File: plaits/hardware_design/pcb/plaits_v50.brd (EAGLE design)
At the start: 59 x 106.7 mm, 162 parts, among them IC1 R-78E3.3-0.5, IC2 TLC59281DBQ, IC3 LD2981ABU33, IC4 STM32F373CCT6, IC5 PCM5100APW, IC6 MCP6004, IC7 MCP6004, IC8 TL072PW, IC9 LM4040B10, J1 PJ301_THONKICONN6, J10 PJ301_THONKICONN6, J2 PJ301_THONKICONN6, J3 PJ301_THONKICONN6, J4 PJ301_THONKICONN6, J5 PJ301_THONKICONN6, J6 PJ301_THONKICONN6, J7 PJ301_THONKICONN6, J8 PJ301_THONKICONN6, J9 PJ301_THONKICONN6, Q1 8MHz

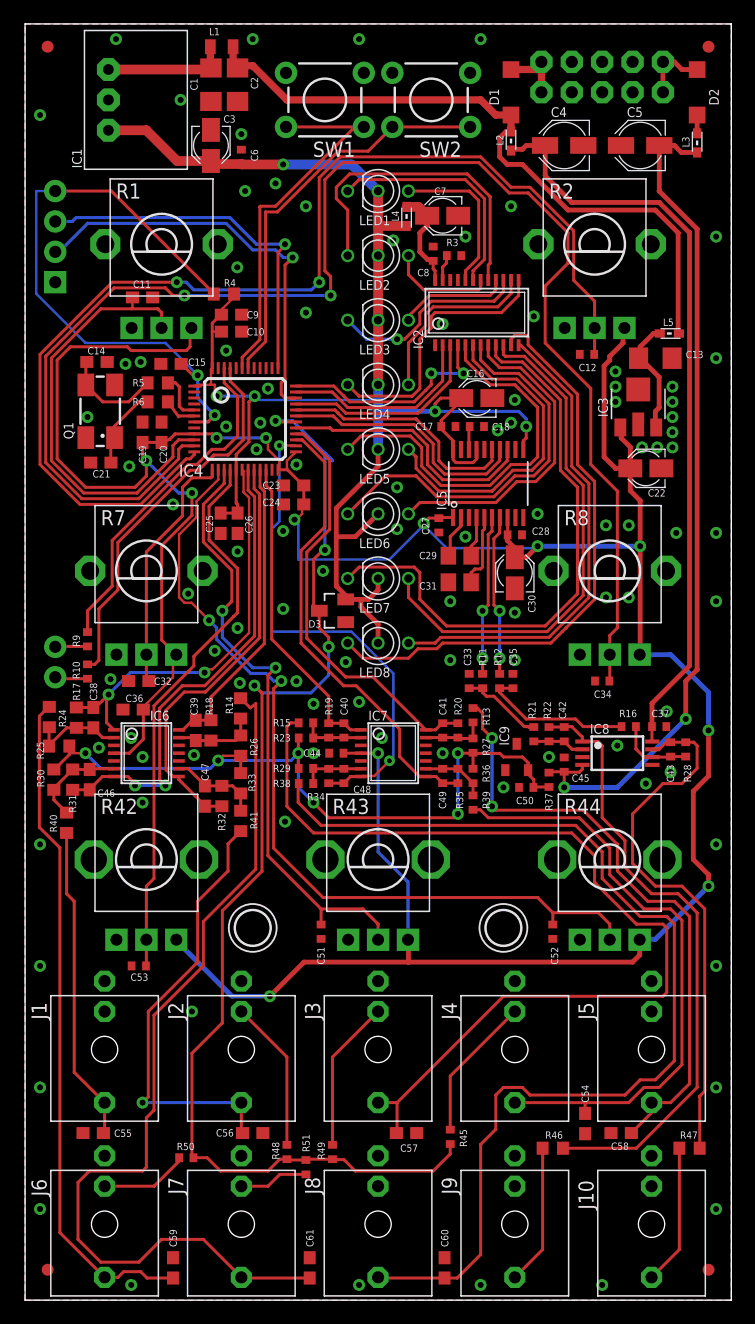
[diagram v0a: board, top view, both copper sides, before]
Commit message: converting mini packages to 603, all done, CRC check ok.
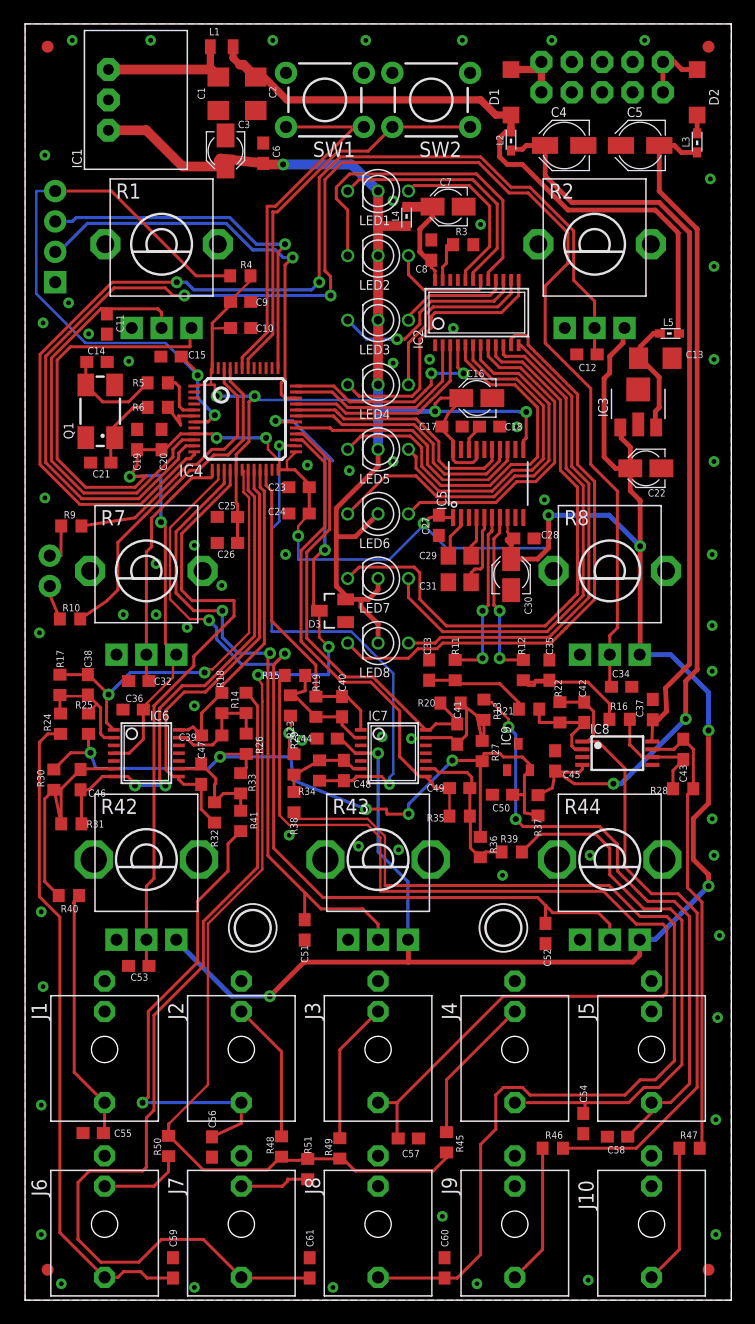
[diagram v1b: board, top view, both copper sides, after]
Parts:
- C12, C17, C18, C27, C28, C33, C34, C35, C37, C40, C41, C42, C43, C44, C45, C48, C49, C50, C51, C52, C53, C6, C8: device rcl:C0402 -> rcl:C0603
- R10, R11, R12, R13, R15, R16, R19, R20, R21, R22, R23, R27, R28, R29, R3, R34, R35, R36, R37, R38, R39, R45, R48, R49, R50, R51, R9: device rcl:R0402 -> rcl:R0603
- moved R9 9.56 mm to (3.89, 64.7), turned to 0 degrees
- moved JP5 7.63 mm to (2.08, 62.2)
- moved R40 6.09 mm to (3.68, 33.8), turned to 0 degrees
- moved R36 5.97 mm to (38.1, 37.9)
- moved R39 5.25 mm to (40.7, 37.5), turned to 0 degrees
- moved R10 4.63 mm to (3.78, 56.9), turned to 0 degrees
- moved R15 4.07 mm to (22.6, 52.2)
- moved C11 3.72 mm to (6.86, 81.6), turned to 270 degrees
- moved R31 3.70 mm to (3.89, 39.8), turned to 180 degrees
- moved C56 3.60 mm to (15.6, 12.8), turned to 270 degrees
- moved C33 3.48 mm to (33.8, 52.7)
- moved R35 3.36 mm to (36.3, 40.5), turned to 0 degrees
- moved R28 3.30 mm to (55.0, 42.7), turned to 180 degrees
- moved C35 3.18 mm to (43.8, 52.7)
- moved R25 3.08 mm to (5.32, 48.2), turned to 270 degrees
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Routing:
- net N$37: track 8.17 -> 20.8 mm
- net AREF_-10: track 62.4 -> 73.6 mm
- net +3V3_A: track 260.2 -> 269.2 mm
- net N$32: track 5.52 -> 13.2 mm
- net N$41: track 5.37 -> 12.5 mm
- net RX: track 28.7 -> 22.1 mm
- net N$60: track 44.9 -> 38.3 mm
- net +3V3: track 142.0 -> 148.3 mm
- net FM_IN: track 81.0 -> 87.2 mm
- net MODEL_IN: track 26.4 -> 21.1 mm
- net N$34: track 5.27 -> 10.3 mm
- net MORPH_IN: track 50.8 -> 46.6 mm
- net MORPH_ATT: track 71.5 -> 75.5 mm
- net N$62: track 4.33 -> 8.26 mm
- net TIMBRE_ATT: track 46.4 -> 50.2 mm
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
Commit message: Added some signal text, this one works.
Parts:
- moved C48 0.15 mm to (26.5, 44.3)
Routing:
- net N$8: track 3.93 -> 2.61 mm
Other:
- board text added: "C"
- board text added: "D"
- board text added: "R"
- board text added: "rx"
- board text added: "tx"
